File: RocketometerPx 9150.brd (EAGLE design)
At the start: 55.9 x 22.9 mm, 48 parts, among them J001 USB_MICROB_JST, J301 JST 2mm, J401 M07, J701 MICROSD-SOCKET, U101 BMP180, U201 3.3V, U3 EEPROM-I2CEIAJ, U301 MCP73831, U601 MPU6050, U901 ADXL377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

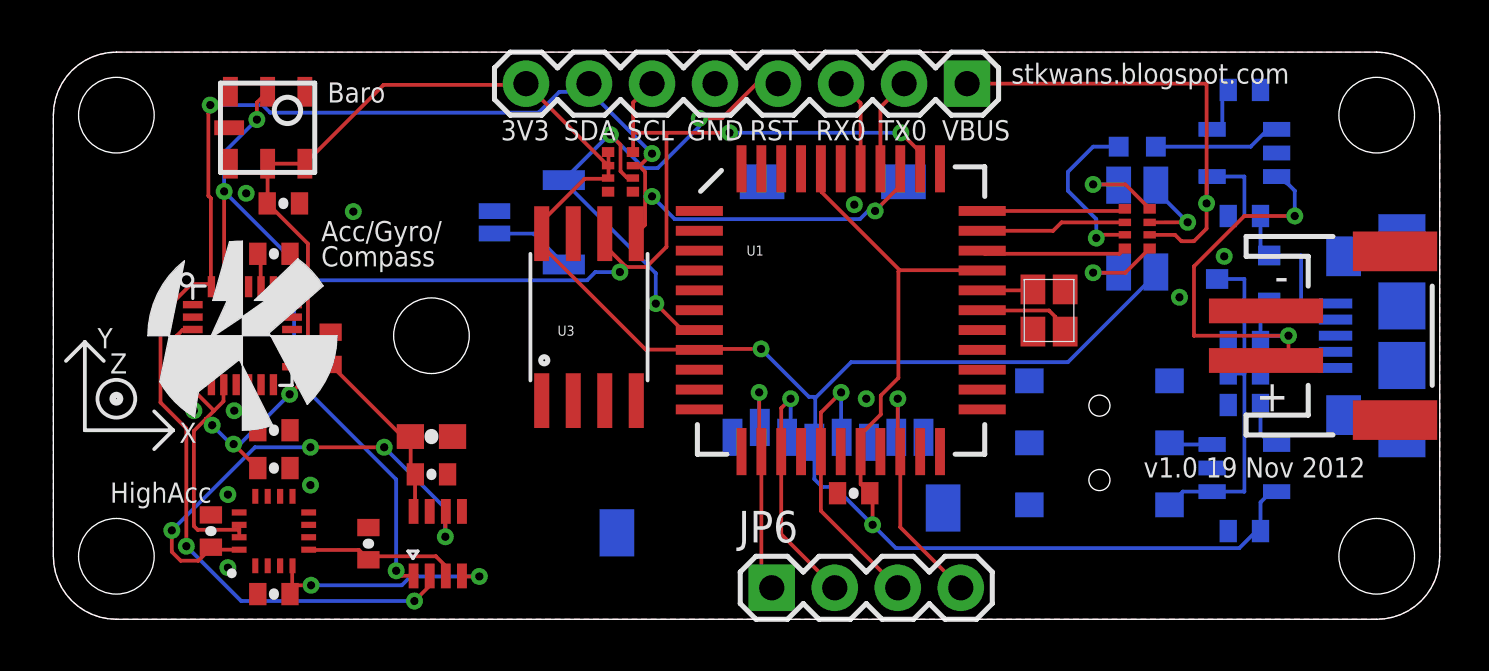
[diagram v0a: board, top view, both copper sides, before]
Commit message: Lots of changes to BPlane. Added bypass caps to RxPx
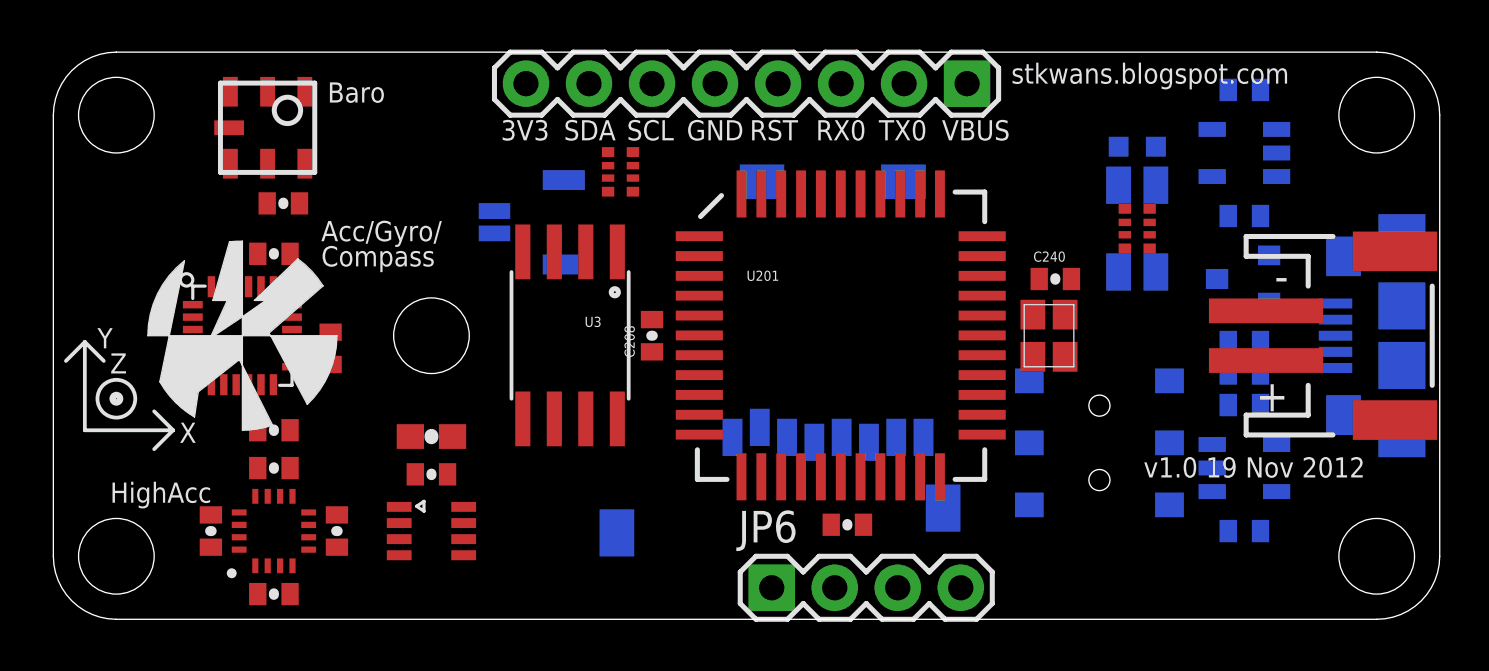
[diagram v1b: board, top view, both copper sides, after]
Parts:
- removed U1: (no value), SparkFun-DigitalIC:P8X32A-Q44
- removed U301: MCP73831, KwanSystems:SOT-23-5
- removed U902: AD7991, KwanSystems:SOT-23-8
- added C208: 1uF, SparkFun:0402-CAP
- added C240: 100nF, SparkFun:0402-CAP
- added U102: 3.3V, KwanSystems:SOT-23-5
- added U401: BMP180, KwanSystems:BMP180
- added U403: AD7991, KwanSystems:SOT-23-8
- C704: value 100nF -> 1uF
- U101: value BMP180 -> MCP73831; device KwanSystems:BMP180 -> KwanSystems:SOT-23-5
- U201: value 3.3V -> (none); device KwanSystems:SOT-23-5 -> SparkFun-DigitalIC:P8X32A-Q44
- moved U101 39.4 mm to (48.0, 18.8), flipped to the bottom, turned to 270 degrees
- moved U201 17.1 mm to (31.8, 11.4), flipped to the top, turned to 0 degrees
- moved C905 1.37 mm to (11.4, 3.56)
- moved C704 1.30 mm to (32.0, 3.81)
- moved U3 1.08 mm to (20.8, 11.4), turned to 180 degrees
- moved Y1 1.02 mm to (40.1, 11.4)
- renumbered D301 to D101, D302 to D102, J001 to J101, J301 to J102, U601 to U404, U901 to U402
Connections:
- removed net P10: U1.11
- net ACCINT: now also U201.11
- net CS: now also U201.13; no longer U1.13
- net GND: now also C208.2, C240.2, U101.2, U102.2, U201.17, U201.27, U201.39, U201.5, U201.6, U401.7, U403.7; no longer U1.17, U1.27, U1.39, U1.5, U1.6, U101.7, U201.2, U301.2, U902.7
- net MISO: now also U201.20; no longer U1.20
- net MOSI: now also U201.14; no longer U1.14
- net N$17: now also U102.4; no longer U201.4
- net N$2: now also U101.5; no longer U301.5
- net N$4: now also U101.1; no longer U301.1
- net P0: now also U201.41; no longer U1.41
- net P1: now also U201.42; no longer U1.42
- net P11: now also U201.12; no longer U1.12
- net P14: now also U201.15; no longer U1.15
- net P16: now also U201.19; no longer U1.19
- net P18: now also U201.21; no longer U1.21
- net P19: now also U201.22; no longer U1.22
- net P2: now also U201.43; no longer U1.43
- net P20: now also U201.23; no longer U1.23
- net P21: now also U201.24; no longer U1.24
- net P22: now also U201.25; no longer U1.25
- net P23: now also U201.26; no longer U1.26
- net P27: now also U201.34; no longer U1.34
- net P3: now also U201.44; no longer U1.44
- net P4: now also U201.1; no longer U1.1
- net P5: now also U201.2; no longer U1.2
- net P6: now also U201.3; no longer U1.3
- net P7: now also U201.4; no longer U1.4
- net P8: now also U201.9; no longer U1.9
- net P9: now also U201.10; no longer U1.10
- net PWMB: now also U201.32; no longer U1.32
- net PWMG: now also U201.33; no longer U1.33
- net PWMR: now also U201.31; no longer U1.31
- net PWR_EN: now also U102.3; no longer U201.3
- net RES: now also U201.7; no longer U1.7
- net RX: now also U201.38; no longer U1.38
- net SCK: now also U201.16; no longer U1.16
- net SCL: now also R401.3, U201.35, U401.5, U403.1; no longer R401.4, U1.35, U101.5, U902.1
- net SDA: now also R401.4, U201.36, U401.6, U403.2; no longer R401.3, U1.36, U101.6, U902.2
- net TX: now also U201.37; no longer U1.37
- net VBUS: now also U101.4; no longer U301.4
- net VCC: now also C208.1, C240.1, U102.5, U201.18, U201.30, U201.40, U201.8, U401.2, U401.3, U403.8; no longer U1.18, U1.30, U1.40, U1.8, U101.2, U101.3, U201.5, U902.8
- net VIN: now also U102.1; no longer U201.1
- net VLIPO: now also U101.3; no longer U301.3
- net XACC: now also U403.3; no longer U902.3
- net XI: now also U201.28; no longer U1.28
- net XO: now also U201.29; no longer U1.29
- net YACC: now also U403.4; no longer U902.4
- net ZACC: now also U403.6; no longer U902.6
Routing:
- net VCC: track 134.8 -> 0.00 mm, vias 5 -> 0
- net SDA: track 68.0 -> 0.00 mm, vias 6 -> 0
- net SCL: track 65.0 -> 0.00 mm, vias 6 -> 0
- net VBUS: track 29.3 -> 0.00 mm, vias 1 -> 0
- net RES: track 22.5 -> 0.00 mm, vias 3 -> 0
- net ZACC: track 19.6 -> 0.00 mm, vias 4 -> 0
- net VLIPO: track 18.7 -> 0.00 mm, vias 2 -> 0
- net VIN: track 13.6 -> 0.00 mm
- net SCK: track 11.3 -> 0.00 mm, vias 1 -> 0
- net MISO: track 10.3 -> 0.00 mm, vias 1 -> 0
- net MOSI: track 10.3 -> 0.00 mm, vias 1 -> 0
- net YACC: track 9.92 -> 0.00 mm, vias 2 -> 0
- net CS: track 9.52 -> 0.00 mm, vias 1 -> 0
- net N$5: track 6.81 -> 0.00 mm, vias 1 -> 0
- net XACC: track 6.44 -> 0.00 mm
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- removed copper zone on layer 1, net GND
- removed copper zone on layer 16, net GND

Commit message: Fixed author information
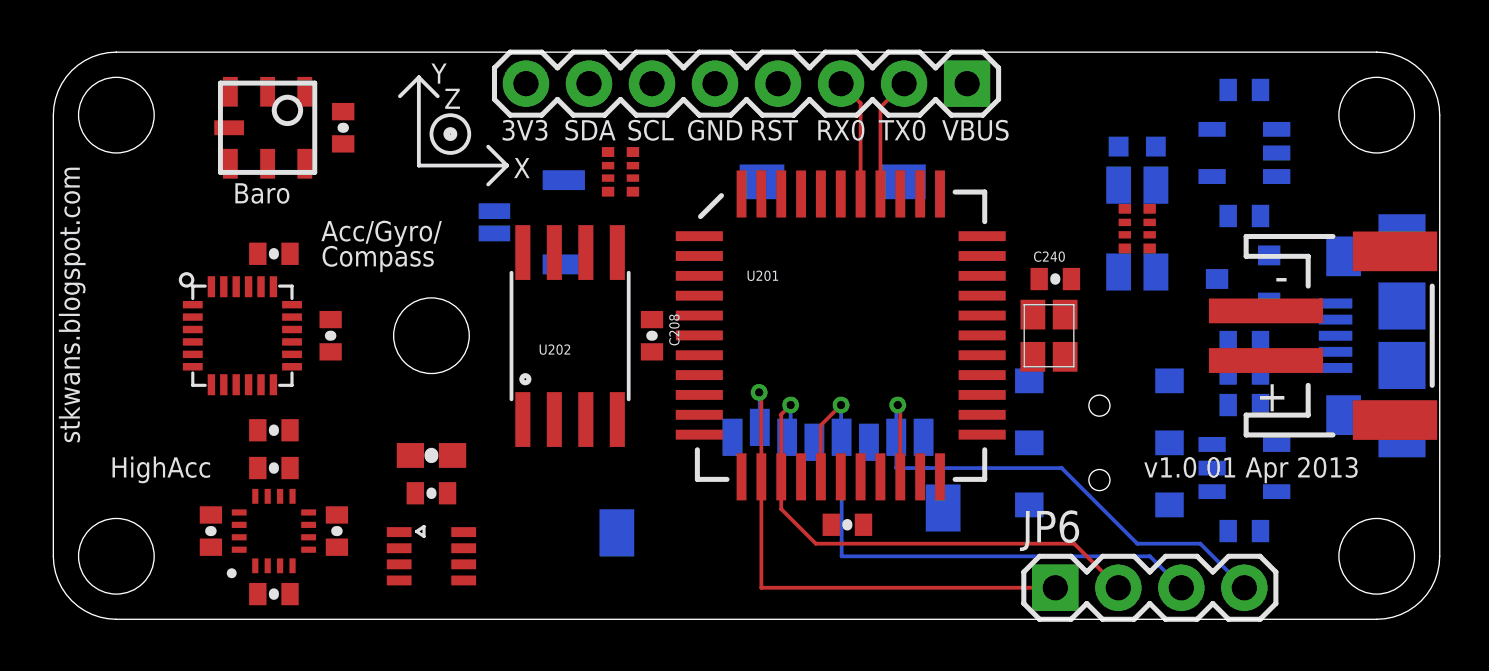
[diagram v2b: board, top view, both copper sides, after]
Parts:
- removed U$1: (no value), KwanSystems:KWAN_ACC
- U$2: value AZ2020 -> AYZ0202; device KwanSystems:AZ2020 -> KwanSystems:AYZ0202
- moved U$4 17.2 mm to (14.7, 18.3)
- moved JP6 11.4 mm to (40.4, 1.27)
- moved C101 3.89 mm to (11.7, 19.8), turned to 90 degrees
- moved U403 1.02 mm to (15.2, 2.54)
- moved C907 0.76 mm to (15.2, 5.08), turned to 180 degrees
- moved C908 0.76 mm to (15.2, 6.60), turned to 180 degrees
- moved C613 0.51 mm to (11.2, 11.4)
- turned C208 to 270 degrees
- turned U202 to 0 degrees
- renumbered C704 to C218, U3 to U202
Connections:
- net SCL: now also J401.7, R401.4; no longer J401.6, R401.3
- net SDA: now also J401.6, R401.3; no longer J401.7, R401.4
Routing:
- net SCK: track 0.00 -> 23.6 mm, vias 0 -> 1
- net MISO: track 0.00 -> 21.5 mm, vias 0 -> 1
- net CS: track 0.00 -> 21.2 mm, vias 0 -> 1
- net MOSI: track 0.00 -> 20.6 mm, vias 0 -> 1
- net TX: track 0.00 -> 4.84 mm
- net RX: track 0.00 -> 4.77 mm
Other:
- board text added: "RocketometerPX9150"
- board text added: "v1.0 01 Apr 2013"
- board text removed: "Boot"
- board text removed: "RocketometerMPU6050"
- board text removed: "v1.0 19 Nov 2012"

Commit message: Rotated Px chip 90deg and rerouted 90% manually
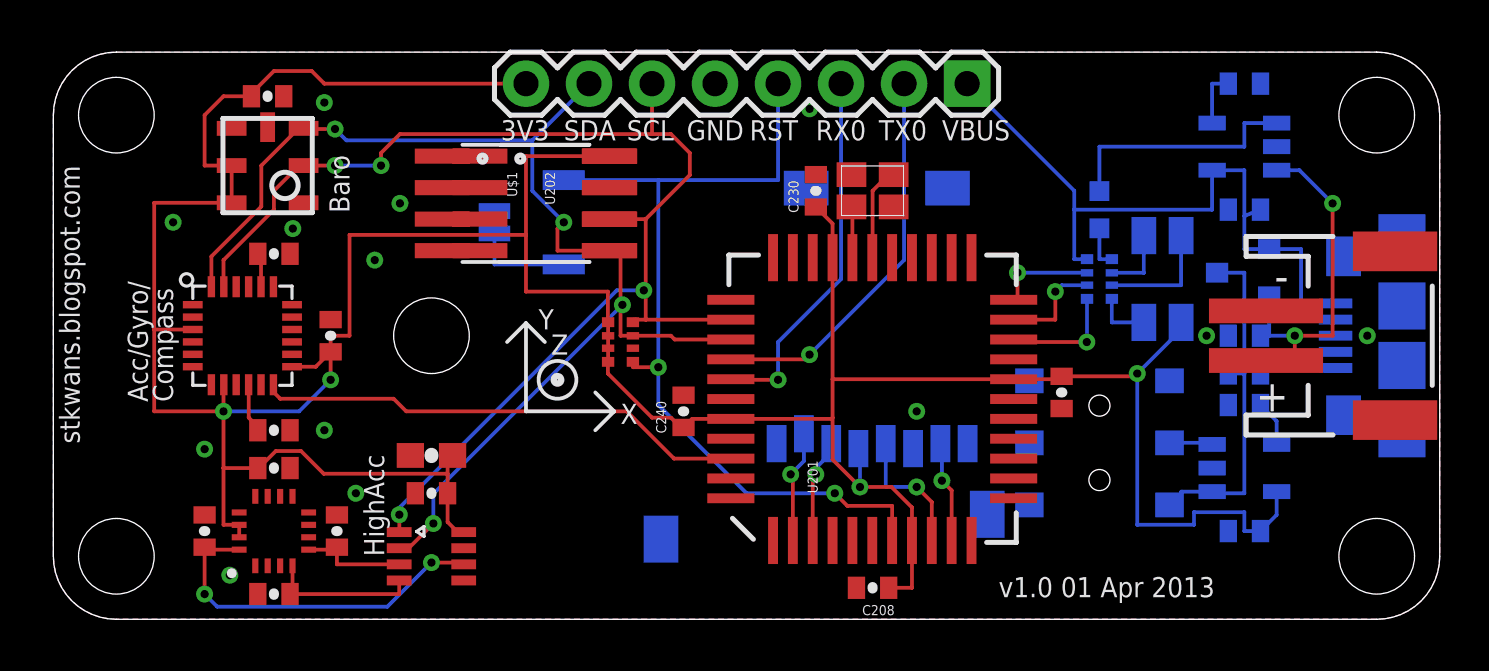
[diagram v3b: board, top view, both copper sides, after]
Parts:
- removed JP6: (no value), SparkFun-Connectors:1X04
- added C230: 100nF, SparkFun:0402-CAP
- added U$1: EEPROM-I2CEIAJ, KwanSystems:SO08-EIAJ
- U201: value (none) -> P8X32A-Q44; device SparkFun-DigitalIC:P8X32A-Q44 -> KwanSystems:P8X32A-Q44
- U202: value EEPROM-I2CEIAJ -> 128kiB; device SparkFun-DigitalIC:SO08-EIAJ -> KwanSystems:SO8N
- moved C240 15.9 mm to (25.4, 8.38), turned to 90 degrees
- moved C208 13.5 mm to (33.0, 1.27), turned to 180 degrees
- moved U$4 10.8 mm to (19.1, 8.38)
- moved C218 10.2 mm to (40.6, 9.14), turned to 270 degrees
- moved Y1 9.20 mm to (33.0, 17.3), turned to 0 degrees
- moved R401 6.86 mm to (22.9, 11.2)
- moved U202 5.43 mm to (19.8, 16.8), turned to 270 degrees
- moved C101 3.30 mm to (8.64, 21.1), turned to 0 degrees
- moved D101 2.96 mm to (42.2, 16.5), turned to 0 degrees
- moved U201 2.84 mm to (33.0, 8.89), turned to 90 degrees
- moved R402 2.54 mm to (42.2, 13.7), flipped to the bottom
- moved D401 2.27 mm to (44.7, 13.7)
- moved J701 1.80 mm to (38.1, 17.8)
- moved U401 1.52 mm to (8.64, 18.3), turned to 90 degrees
- moved C302 0.25 mm to (48.0, 16.5)
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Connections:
- removed net CS: J701.2, JP6.1, U201.13
- removed net MISO: J701.7, JP6.4, U201.20
- removed net MOSI: J701.3, JP6.2, U201.14
- removed net P0: U201.41
- removed net P1: U201.42
- removed net P11: U201.12
- removed net P14: U201.15
- removed net P16: U201.19
- removed net P18: U201.21
- removed net P19: U201.22
- removed net P2: U201.43
- removed net P20: U201.23
- removed net P21: U201.24
- removed net P22: U201.25
- removed net P23: U201.26
- removed net P27: U201.34
- removed net P3: U201.44
- removed net P4: U201.1
- removed net P5: U201.2
- removed net P6: U201.3
- removed net P7: U201.4
- removed net P8: U201.9
- removed net P9: U201.10
- new net CS/DAT3: J701.2, U201.2
- new net DAT1: J701.8
- new net DAT2: J701.1
- new net MISO/DAT0: J701.7, U201.10
- new net MOSI/CMD: J701.3, U201.3
- net ACCINT: now also U201.42; no longer U201.11
- net GND: now also C230.2, U$1.1, U$1.2, U$1.3, U$1.4, U$1.7
- net N$5: now also R402.1; no longer R402.3
- net PWMB: now also R402.6, U201.21; no longer R402.2, U201.32
- net PWMG: now also R402.7, U201.22; no longer R402.1, U201.33
- net PWMR: now also R402.5, U201.20; no longer R402.4, U201.31
- net QWMB: now also R402.3; no longer R402.7
- net QWMG: now also R402.2; no longer R402.8
- net QWMR: now also R402.4; no longer R402.5
- net RES: now also R401.1; no longer R401.2
- net SCK: now also U201.9; no longer JP6.3, U201.16
- net SCL: now also J401.6, U$1.6; no longer J401.7
- net SDA: now also J401.7, U$1.5; no longer J401.6
- net VBUS: now also R402.8; no longer R402.6
- net VCC: now also C230.1, R401.8, U$1.8
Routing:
- net VCC: track 0.00 -> 150.4 mm, vias 0 -> 4
- net SCL: track 0.00 -> 52.8 mm, vias 0 -> 4
- net SDA: track 0.00 -> 50.1 mm, vias 0 -> 4
- net RES: track 0.00 -> 35.3 mm, vias 0 -> 2
- net VBUS: track 0.00 -> 27.6 mm
- net MISO: track 21.5 -> 0.00 mm, vias 1 -> 0
- net CS: track 21.2 -> 0.00 mm, vias 1 -> 0
- net MOSI: track 20.6 -> 0.00 mm, vias 1 -> 0
- net ACCINT: track 0.00 -> 19.8 mm
- net SCK: track 23.6 -> 5.40 mm
- net ZACC: track 0.00 -> 15.3 mm, vias 0 -> 2
- net VLIPO: track 0.00 -> 15.1 mm, vias 0 -> 2
- net VIN: track 0.00 -> 13.9 mm
- net TX: track 4.84 -> 15.8 mm, vias 0 -> 1
- net RX: track 4.77 -> 14.9 mm, vias 0 -> 1
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- added copper zone on layer 1, net GND
- added copper zone on layer 16, net GND
